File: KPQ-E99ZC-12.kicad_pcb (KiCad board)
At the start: 2 copper layers, 79 x 50.7 mm, 23 parts, among them J1 USB, J2 Chassis, J3 SWD, J4 Edge Connector, J5 Alternate Connector, SW1 BOOT, U1 USBLC6-2SC6, U2 XC6206P332MR-G, U3 STM32C071KBT6

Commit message: Tweak routing
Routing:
- net GND: track 38.7 -> 68.6 mm, vias 16 -> 17
- net NRST: track 40.4 -> 39.3 mm, vias 1 -> 2
- net +5V: track 144.5 -> 143.8 mm
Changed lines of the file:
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@@
 	)
 	(segment
-		(start 127.8732 120.8)
-		(end 129.806 118.8672)
+		(start 98 128)
+		(end 99.032 128)
+		(width 0.4)
+		(layer "F.Cu")
+		(net 1)
+	)
+	(segment
+		(start 129.806 117.752)
+		(end 129.806 120.066)
 		(width 0.4)
 		(layer "F.Cu")
@@
 	)
 	(segment
-		(start 126.4 120.8)
-		(end 127.8732 120.8)
-		(width 0.4)
-		(layer "F.Cu")
-		(net 1)
-	)
-	(segment
-		(start 99.6 125.825)
-		(end 99.6 119.2892)
-		(width 0.4)
-		(layer "F.Cu")
-		(net 1)
-	)
-	(segment
 		(start 98.8625 142.2965)
 		(end 98.8625 143.754)
@@
 	)
 	(segment
+		(start 99.032 128)
+		(end 99.6 127.432)
+		(width 0.4)
+		(layer "F.Cu")
+		(net 1)
+	)
+	(segment
+		(start 99.6 117.1344)
+		(end 100.7324 116.002)
+		(width 0.4)
+		(layer "F.Cu")
+		(net 1)
+	)
+	(segment
 		(start 97.714 141.148)
 		(end 98.8625 142.2965)
@@
 	)
 	(segment
-		(start 129.806 118.8672)
-		(end 129.806 117.752)
-		(width 0.4)
-		(layer "F.Cu")
-		(net 1)
-	)
-	(segment
 		(start 102.2824 121.2704)
 		(end 102.2824 119.558)
@@
 		(start 87.806 117.752)
 		(end 87.806 119.53)
+		(width 0.4)
+		(layer "F.Cu")
+		(net 1)
+	)
+	(segment
+		(start 99.6 125.825)
+		(end 99.6 117.1344)
 		(width 0.4)
 		(layer "F.Cu")
@@
 	)
 	(via
-		(at 126.4 120.8)
+		(at 129.806 120.066)
 		(size 0.8)
 		(drill 0.5)
@@
 	)
 	(via
+		(at 124.446 118.669)
+		(size 0.8)
+		(drill 0.5)
+		(layers "F.Cu" "B.Cu")
+		(net 1)
+	)
+	(via
 		(at 97.714 141.148)
 		(size 0.8)
@@
 		(drill 0.5)
 		(layers "F.Cu" "B.Cu")
+		(net 1)
+	)
+	(segment
+		(start 120.78 142.773355)
+		(end 102 132)
+		(width 0.4)
+		(layer "B.Cu")
+		(net 1)
+	)
+	(segment
+		(start 102 132)
+		(end 98 128)
+		(width 0.4)
+		(layer "B.Cu")
 		(net 1)
 	)
@@
 	)
 	(segment
+		(start 124.446 120.8)
+		(end 132.893 123.65)
+		(width 0.4)
+		(layer "F.Cu")
+		(net 2)
+	)
+	(segment
 		(start 103.556 143.434)
 		(end 103.556 144.704)
@@
 	)
 	(segment
-		(start 127.296 123.65)
-		(end 134.798 123.65)
-		(width 0.4)
-		(layer "F.Cu")
-		(net 2)
-	)
-	(segment
 		(start 101.1375 144.704)
 		(end 103.556 144.704)
@@
 	)
 	(segment
-		(start 124.446 120.8)
-		(end 127.296 123.65)
+		(start 132.893 123.65)
+		(end 134.798 123.65)
 		(width 0.4)
 		(layer "F.Cu")
@@
 		(width 0.2)
 		(layer "F.Cu")
+		(net 4)
+	)
+	(segment
+		(start 124.446 123.876)
+		(end 134.798 126.19)
+		(width 0.2)
+		(layer "F.Cu")
+		(net 4)
+	)
+	(via
+		(at 124.446 123.876)
+		(size 0.5)
+		(drill 0.3)
+		(layers "F.Cu" "B.Cu")
 		(net 4)
 	)
@@
 	)
 	(segment
-		(start 105.08 126.924)
-		(end 115.748 126.924)
-		(width 0.2)
-		(layer "B.Cu")
-		(net 4)
-	)
-	(segment
-		(start 115.748 126.924)
-		(end 118.542 126.19)
-		(width 0.2)
-		(layer "B.Cu")
-		(net 4)
-	)
-	(segment
-		(start 118.542 126.19)
-		(end 134.798 126.19)
-		(width 0.2)
-		(layer "B.Cu")
-		(net 4)
-	)
-	(segment
 		(start 98.8 123.876)
-		(end 102.032 123.876)
-		(width 0.2)
-		(layer "B.Cu")
-		(net 4)
-	)
-	(segment
-		(start 102.032 123.876)
-		(end 105.08 126.924)
+		(end 124.446 123.876)
 		(width 0.2)
 		(layer "B.Cu")
@@
 	)
 	(segment
-		(start 106.879 125.167)
-		(end 106.221 125.825)
-		(width 0.2)
-		(layer "F.Cu")
-		(net 34)
-	)
-	(segment
 		(start 106.221 125.825)
 		(end 102.8 125.825)
@@
 	)
 	(via
-		(at 106.879 125.167)
+		(at 106.221 125.825)
 		(size 0.5)
 		(drill 0.3)
@@
 	)
 	(segment
-		(start 108.424 123.622)
-		(end 129.244 123.622)
-		(width 0.2)
-		(layer "B.Cu")
-		(net 34)
-	)
-	(segment
-		(start 106.879 125.167)
-		(end 108.424 123.622)
+		(start 106.221 125.825)
+		(end 127.041 125.825)
 		(width 0.2)
 		(layer "B.Cu")
@@
 	)
 	(segment
-		(start 129.244 123.622)
+		(start 127.041 125.825)
 		(end 132.066 120.8)
 		(width 0.2)

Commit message: Fix DRC errors
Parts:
- moved R2 1.65 mm to (130.4, 120.8)
- moved J2 0.70 mm to (132.7, 106.0)
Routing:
- net LED: track 42.2 -> 39.8 mm
- net +5V: track 143.8 -> 145.1 mm
- net GND: track 68.6 -> 69.6 mm
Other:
- outline, holes or cut-outs redrawn

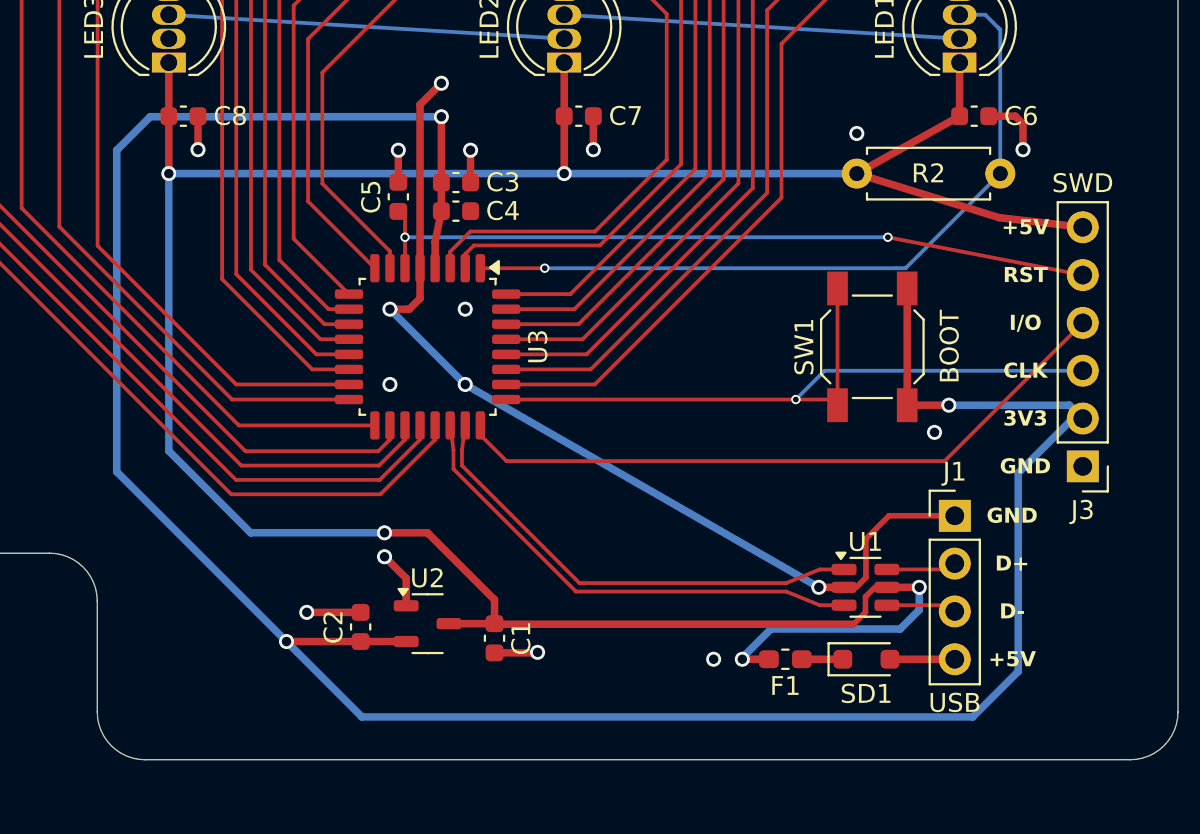
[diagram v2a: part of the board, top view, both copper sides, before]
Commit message: Flip boot switch to back
This should be accessible through existing holes in the case near the tilt legs.
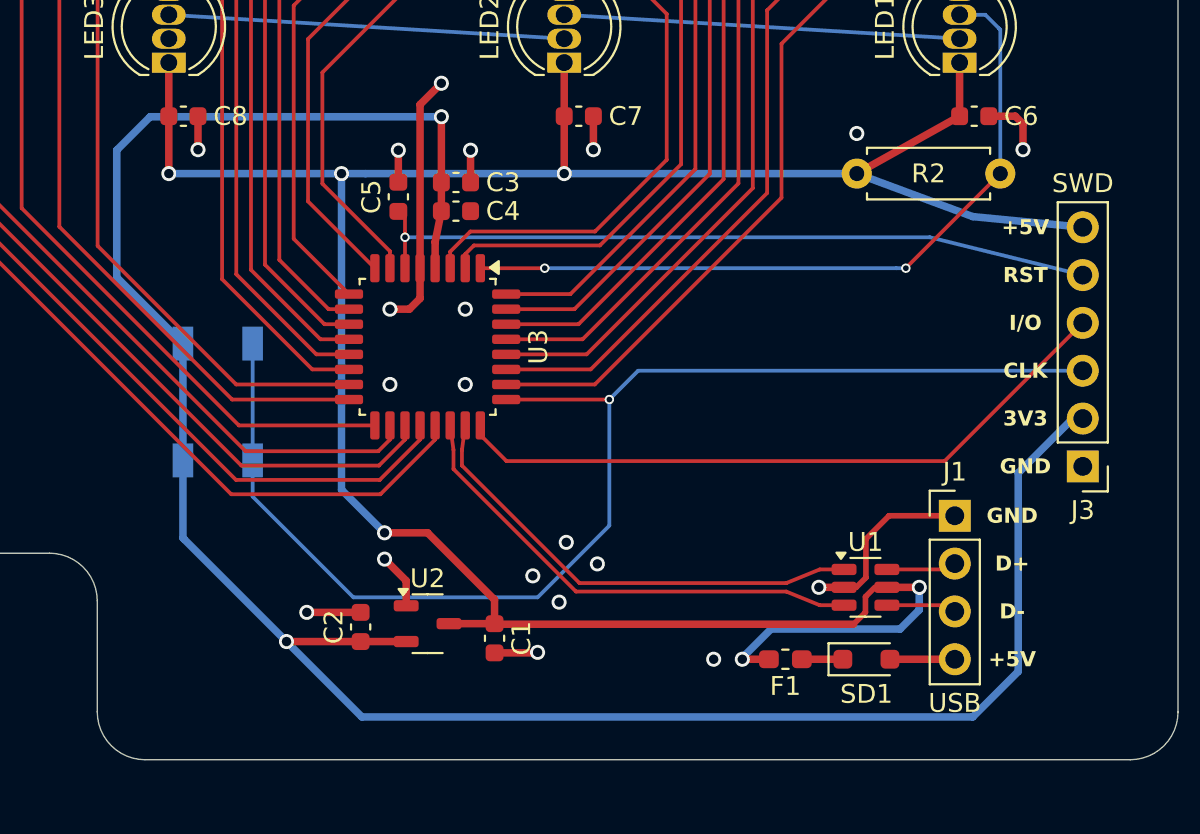
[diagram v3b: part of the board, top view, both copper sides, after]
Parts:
- SW1: moved to B.Cu
- moved SW1 34.9 mm to (88.9, 132.9)
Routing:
- net BOOT0/SWCLK: track 39.8 -> 68.8 mm
- net GND: track 69.6 -> 42.2 mm, vias 17 -> 20
- net +3V3: track 134.8 -> 118.9 mm, vias 3 -> 2
- net +5V: track 145.1 -> 137.2 mm, vias 5 -> 6
- net NRST: track 39.2 -> 39.3 mm, vias 2 -> 1
- net LED: track 39.8 -> 39.9 mm, vias 1 -> 2

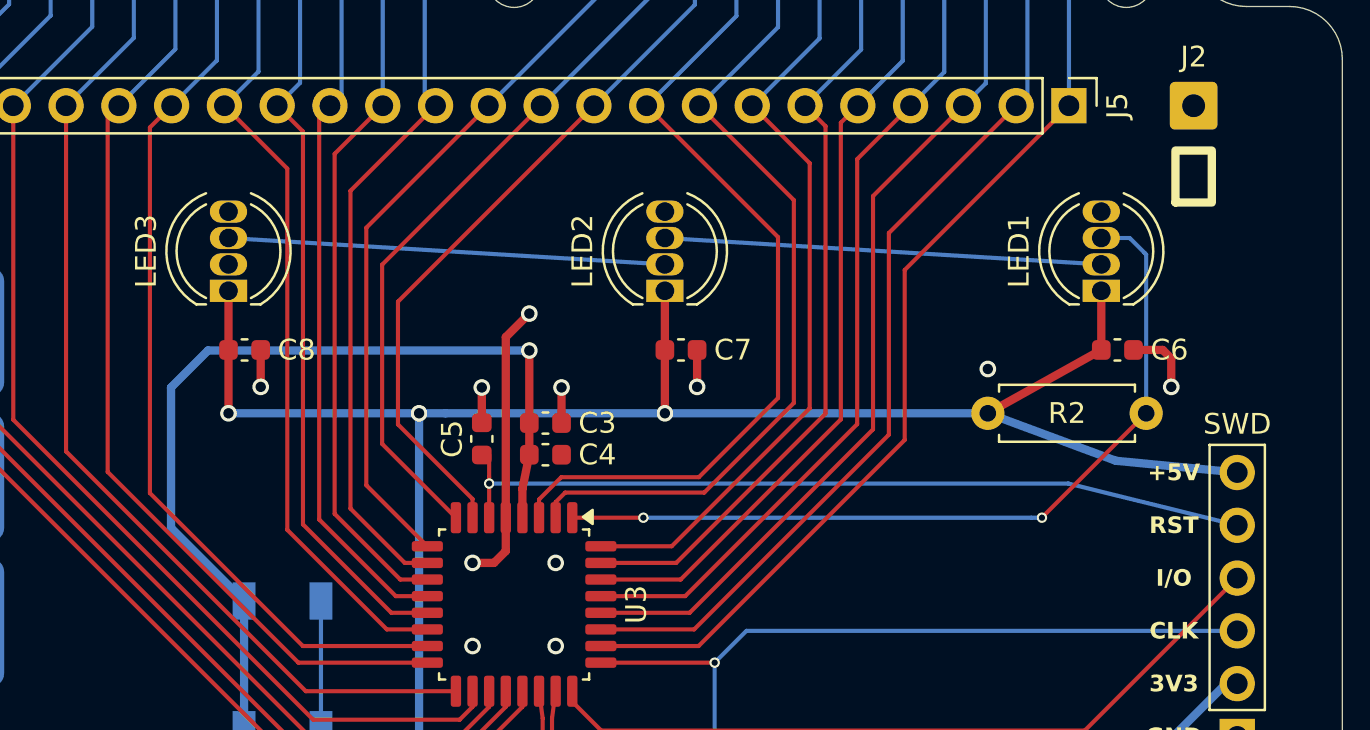
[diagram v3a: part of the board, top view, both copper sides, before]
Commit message: Rotate LEDs
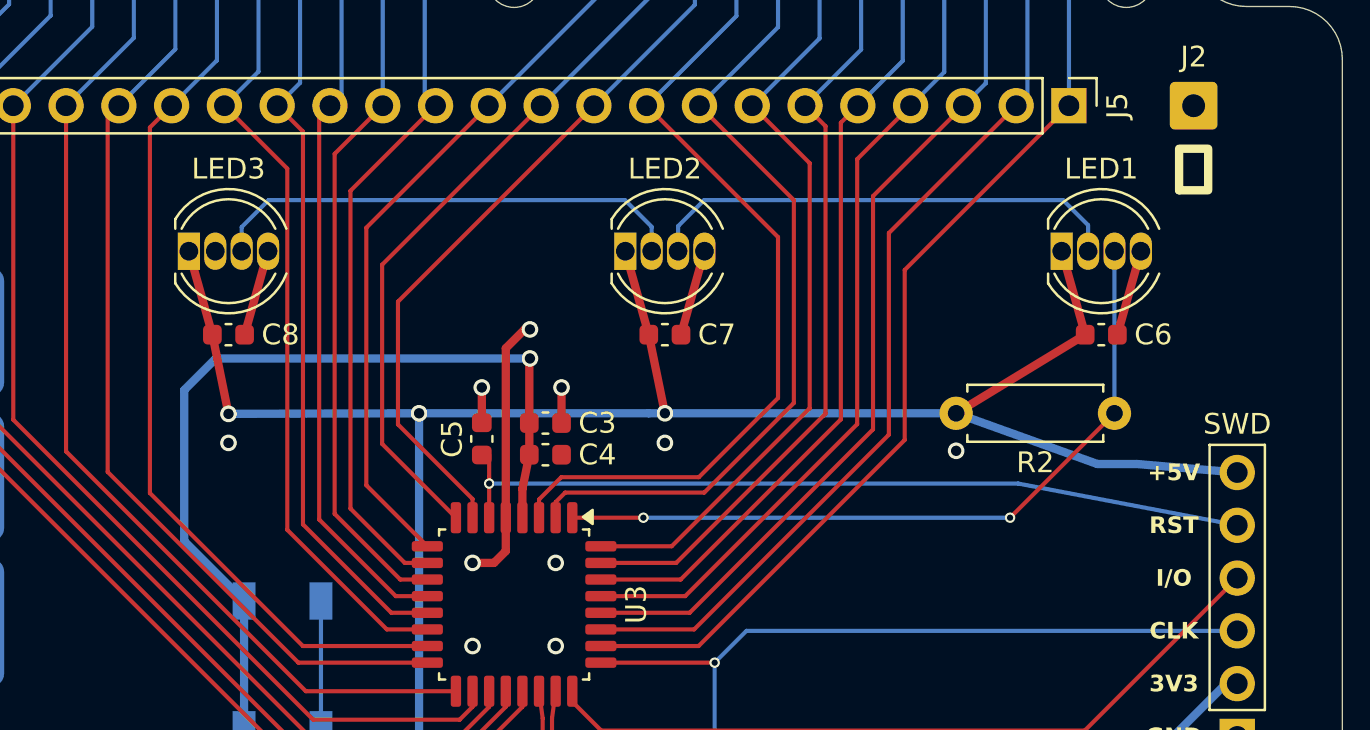
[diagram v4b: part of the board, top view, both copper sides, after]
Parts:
- moved LED1 2.69 mm to (126.4, 113.0), turned to 0 degrees
- moved LED2 2.69 mm to (105.4, 113.0), turned to 0 degrees
- moved LED3 2.69 mm to (84.4, 113.0), turned to 0 degrees
- moved R2 1.53 mm to (128.9, 120.8)
- moved C6 1.07 mm to (128.3, 117.0)
- moved C7 1.07 mm to (107.3, 117.0)
- moved C8 1.07 mm to (86.3, 117.0)
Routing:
- net +5V: track 137.2 -> 143.9 mm
- net GND: track 42.2 -> 47.2 mm, vias 20 -> 19
- net LED: track 39.9 -> 36.0 mm
- net Net-(LED1-DOUT): track 21.0 -> 23.2 mm
- net Net-(LED2-DOUT): track 21.0 -> 23.1 mm
- net +3V3: track 118.9 -> 117.5 mm

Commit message: Tweak routing
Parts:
- moved R2 1.27 mm to (130.2, 120.8)
- moved J3 0.76 mm to (134.0, 136.3)
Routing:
- net GND: track 47.2 -> 75.5 mm
- net BOOT0/SWCLK: track 68.8 -> 62.0 mm
- net SWDIO: track 36.1 -> 32.4 mm
- net +5V: track 143.9 -> 142.1 mm
- net NRST: track 39.2 -> 38.5 mm
- net LED: track 36.0 -> 36.7 mm
- net +3V3: track 117.5 -> 116.8 mm
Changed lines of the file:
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@@
 	(footprint "Resistor_THT:R_Axial_DIN0207_L6.3mm_D2.5mm_P7.62mm_Horizontal"
 		(layer "F.Cu")
-		(at 128.891 120.8 180)
+		(at 130.161 120.8 180)
 		(descr "Resistor, Axial_DIN0207 series, Axial, Horizontal, pin pitch=7.62mm, 0.25W = 1/4W, length*diameter=6.3*2.5mm^2, http://cdn-reichelt.de/documents/datenblatt/B400/1_4W%23YAG.pdf")
 		(tags "Resistor Axial_DIN0207 series Axial Horizontal pin pitch 7.62mm 0.25W = 1/4W length 6.3mm diameter 2.5mm")
@@
 	(footprint "Project_Library:PinHeader_1x06_P2.54mm_Vertical"
 		(layer "F.Cu")
-		(at 134.798 136.35 180)
+		(at 134.036 136.35 180)
 		(descr "Through hole straight pin header, 1x06, 2.54mm pitch, single row")
 		(tags "Through hole pin header THT 1x06 2.54mm single row")
@@
 	)
 	(segment
-		(start 98 128)
-		(end 99.032 128)
+		(start 99.6 125.825)
+		(end 99.6 127.54)
 		(width 0.4)
 		(layer "F.Cu")
@@
 	)
 	(segment
-		(start 99.032 128)
-		(end 99.6 127.432)
+		(start 100.762 116.764)
+		(end 100.508 116.764)
 		(width 0.4)
 		(layer "F.Cu")
@@
 	)
 	(segment
-		(start 100.762 116.764)
-		(end 100.508 116.764)
+		(start 129.031 117.018)
+		(end 130.161 113)
 		(width 0.4)
 		(layer "F.Cu")
@@
 	)
 	(segment
-		(start 129.031 117.018)
-		(end 130.161 113)
+		(start 99.6 127.54)
+		(end 100.06 128)
 		(width 0.4)
 		(layer "F.Cu")
@@
 	)
 	(segment
-		(start 93.584 144.104)
-		(end 96.444 144.104)
+		(start 100.06 128)
+		(end 102 128)
 		(width 0.4)
 		(layer "F.Cu")
@@
 	)
 	(segment
-		(start 97.714 141.275)
-		(end 98.8625 142.4235)
+		(start 93.584 144.104)
+		(end 96.444 144.104)
 		(width 0.4)
 		(layer "F.Cu")
@@
 	)
 	(segment
-		(start 99.6 125.825)
-		(end 99.6 127.432)
+		(start 97.714 141.275)
+		(end 98.8625 142.4235)
 		(width 0.4)
 		(layer "F.Cu")
@@
 	)
 	(segment
+		(start 105.7658 138.8366)
+		(end 104.3434 137.4142)
+		(width 0.4)
+		(layer "F.Cu")
+		(net 1)
+	)
+	(segment
 		(start 124.508 138.973355)
 		(end 128 138.973355)
@@
 	)
 	(via
-		(at 106.985 143.561)
+		(at 104.0386 140.5638)
 		(size 0.8)
 		(drill 0.5)
@@
 	)
 	(via
-		(at 109.017 141.529)
+		(at 105.7658 138.8366)
 		(size 0.8)
 		(drill 0.5)
@@
 	)
 	(via
-		(at 107.366 140.386)
+		(at 104.3434 137.4142)
 		(size 0.8)
 		(drill 0.5)
@@
 	)
 	(via
-		(at 121.271 122.606)
+		(at 122.541 122.606)
 		(size 0.8)
 		(drill 0.5)
@@
 	)
 	(via
-		(at 105.588 142.164)
+		(at 102.6162 139.1414)
 		(size 0.8)
 		(drill 0.5)
@@
 	)
 	(segment
-		(start 121.271 120.8)
-		(end 127.481 117.018)
+		(start 120.78 142.773355)
+		(end 105.7658 138.8366)
 		(width 0.4)
-		(layer "F.Cu")
-		(net 2)
+		(layer "B.Cu")
+		(net 1)
+	)
+	(segment
+		(start 104.3434 137.4142)
+		(end 102 132)
+		(width 0.4)
+		(layer "B.Cu")
+		(net 1)
+	)
+	(segment
+		(start 102 132)
+		(end 102 128)
+		(width 0.4)
+		(layer "B.Cu")
+		(net 1)
 	)
 	(segment
@@
 	)
 	(segment
+		(start 122.541 120.8)
+		(end 127.481 117.018)
+		(width 0.4)
+		(layer "F.Cu")
+		(net 2)
+	)
+	(segment
 		(start 127.481 117.018)
 		(end 126.351 113)
@@
 	)
 	(segment
+		(start 128.829 123.241)
+		(end 134.036 123.65)
+		(width 0.4)
+		(layer "B.Cu")
+		(net 2)
+	)
+	(segment
 		(start 95.428 120.8)
 		(end 95.428 137.592)
@@
 	)
 	(segment
-		(start 129.972 123.241)
-		(end 134.798 123.65)
-		(width 0.4)
-		(layer "B.Cu")
-		(net 2)
-	)
-	(segment
-		(start 121.271 120.8)
-		(end 128.067 123.241)
-		(width 0.4)
-		(layer "B.Cu")
-		(net 2)
-	)
-	(segment
-		(start 106.481 120.8)
-		(end 121.271 120.8)
+		(start 122.541 120.8)
+		(end 128.829 123.241)
 		(width 0.4)
 		(layer "B.Cu")
@@
 	)
 	(segment
-		(start 128.067 123.241)
-		(end 129.972 123.241)
-		(width 0.4)
-		(layer "B.Cu")
-		(net 2)
-	)
-	(segment
 		(start 86.256 120.828)
 		(end 95.428 120.8)
@@
 	(segment
 		(start 95.428 120.8)
-		(end 106.481 120.8)
+		(end 122.541 120.8)
 		(width 0.4)
 		(layer "B.Cu")
@@
 	)
 	(segment
-		(start 84.125 119.685)
-		(end 84.125 126.949001)
+		(start 131.369 136.477)
+		(end 134.036 133.81)
 		(width 0.4)
 		(layer "B.Cu")
@@
 	)
 	(segment
-		(start 87.079 140.226)
-		(end 87.005999 140.152999)
+		(start 84.125 119.685)
+		(end 84.125 126.949001)
 		(width 0.4)
 		(layer "B.Cu")
@@
 	)
 	(segment
-		(start 134.262 133.81)
-		(end 134.798 133.81)
+		(start 87.005999 140.152999)
+		(end 96.51 149.657)
 		(width 0.4)
 		(layer "B.Cu")
@@
 	)
 	(segment
-		(start 128.956 149.657)
-		(end 131.369 147.244)
+		(start 87.005999 129.83)
+		(end 87.005999 140.152999)
 		(width 0.4)
 		(layer "B.Cu")
@@
 	)
 	(segment
-		(start 85.649 118.161)
-		(end 84.125 119.685)
-		(width 0.4)
-		(layer "B.Cu")
-		(net 3)
-	)
-	(segment
 		(start 96.51 149.657)
 		(end 128.956 149.657)
@@
 	)
 	(segment
-		(start 100.762 118.161)
-		(end 85.649 118.161)
-		(width 0.4)
-		(layer "B.Cu")
-		(net 3)
-	)
-	(segment
-		(start 131.369 136.703)
-		(end 134.262 133.81)
+		(start 85.649 118.161)
+		(end 84.125 119.685)
 		(width 0.4)
 		(layer "B.Cu")
@@
 	)
 	(segment
-		(start 87.079 140.226)
-		(end 96.51 149.657)
+		(start 100.762 118.161)
+		(end 85.649 118.161)
 		(width 0.4)
 		(layer "B.Cu")
@@
 	(segment
 		(start 131.369 147.244)
-		(end 131.369 136.703)
+		(end 131.369 136.477)
 		(width 0.4)
 		(layer "B.Cu")
@@
 	)
 	(segment
-		(start 87.005999 140.152999)
-		(end 87.005999 129.83)
+		(start 128.956 149.657)
+		(end 131.369 147.244)
 		(width 0.4)
 		(layer "B.Cu")
@@
 	(segment
 		(start 124.257 124.1808)
-		(end 134.798 126.19)
+		(end 134.036 126.19)
 		(width 0.2)
 		(layer "B.Cu")
@@
 	)
 	(segment
-		(start 102.8 134.677)
-		(end 104.191 136.068)
-		(width 0.2)
-		(layer "F.Cu")
-		(net 8)
-	)
-	(segment
-		(start 102.8 134.175)
-		(end 102.8 134.677)
-		(width 0.2)
-		(layer "F.Cu")
-		(net 8)
-	)
-	(segment
-		(start 127.46 136.068)
-		(end 134.798 128.73)
+		(start 122.352 134.175)
+		(end 102.8 134.175)
 		(width 0.2)
 		(layer "F.Cu")
@@
 	)
 	(segment
-		(start 104.191 136.068)
-		(end 127.46 136.068)
+		(start 122.352 134.175)
+		(end 134.036 128.73)
 		(width 0.2)
 		(layer "F.Cu")
@@
 	(segment
 		(start 104.175 132.8)
-		(end 109.652 132.8)
+		(end 106.731 132.8)
 		(width 0.2)
 		(layer "F.Cu")
@@
 	)
 	(via
-		(at 109.652 132.8)
+		(at 106.731 132.8)
 		(size 0.5)
 		(drill 0.3)
@@
 	)
 	(segment
-		(start 109.652 132.8)
-		(end 111.182 131.27)
+		(start 106.731 132.751757)
+		(end 106.731 136.449)
 		(width 0.2)
 		(layer "B.Cu")
@@
 	)
 	(segment
-		(start 105.842 143.307)
-		(end 109.652 139.497)
+		(start 106.731 136.449)
+		(end 100.889 142.291)
 		(width 0.2)
 		(layer "B.Cu")
@@
 	)
 	(segment
-		(start 90.706001 137.950001)
-		(end 96.063 143.307)
+		(start 106.731 132.8)
+		(end 134.036 131.27)
 		(width 0.2)
 		(layer "B.Cu")
@@
 	)
 	(segment
-		(start 109.652 139.497)
-		(end 109.652 132.8)
+		(start 90.706001 129.83)
+		(end 90.706001 136.03)
 		(width 0.2)
 		(layer "B.Cu")
@@
 	)
 	(segment
-		(start 90.706001 136.03)
+		(start 95.047 142.291)
 		(end 90.706001 137.950001)
 		(width 0.2)
@@
 	)
 	(segment
-		(start 90.706001 129.83)
-		(end 90.706001 136.03)
+		(start 100.889 142.291)
+		(end 95.047 142.291)
 		(width 0.2)
 		(layer "B.Cu")
@@
 	)
 	(segment
-		(start 111.182 131.27)
-		(end 134.798 131.27)
-		(width 0.2)
-		(layer "B.Cu")
-		(net 9)
-	)
-	(segment
-		(start 96.063 143.307)
-		(end 105.842 143.307)
+		(start 90.706001 137.950001)
+		(end 90.706001 136.03)
 		(width 0.2)
 		(layer "B.Cu")
@@
 	)
 	(segment
-		(start 123.866 125.825)
-		(end 128.891 120.8)
+		(start 122.541 125.825)
+		(end 130.161 120.8)
 		(width 0.2)
 		(layer "F.Cu")
@@
 	)
 	(via
-		(at 123.866 125.825)
+		(at 122.541 125.825)
 		(size 0.5)
 		(drill 0.3)
@@
 	(segment
 		(start 106.221 125.825)
-		(end 123.866 125.825)
+		(end 122.479 125.825)
 		(width 0.2)
 		(layer "B.Cu")
@@
 	)
 	(segment
-		(start 128.891 120.8)
+		(start 130.161 120.8)
 		(end 128.891 113)
 		(width 0.2)
